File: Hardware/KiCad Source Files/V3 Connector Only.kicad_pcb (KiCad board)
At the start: 2 copper layers, 60 x 100 mm, 65 parts, among them J1 YK3210203000G, J2 USB4085-GF-A, J3 Conn_01x08, J4 YK3210203000G, J5 USB4085-GF-A, J6 USB1125-GF-B, Q1 IRLU024NPBF, Q2 IRLU024NPBF, Q3 Q_NMOS, U1 MC33063AP, U4 LM4040LP-2.0, U5 MCP4801, U6 MCP3202

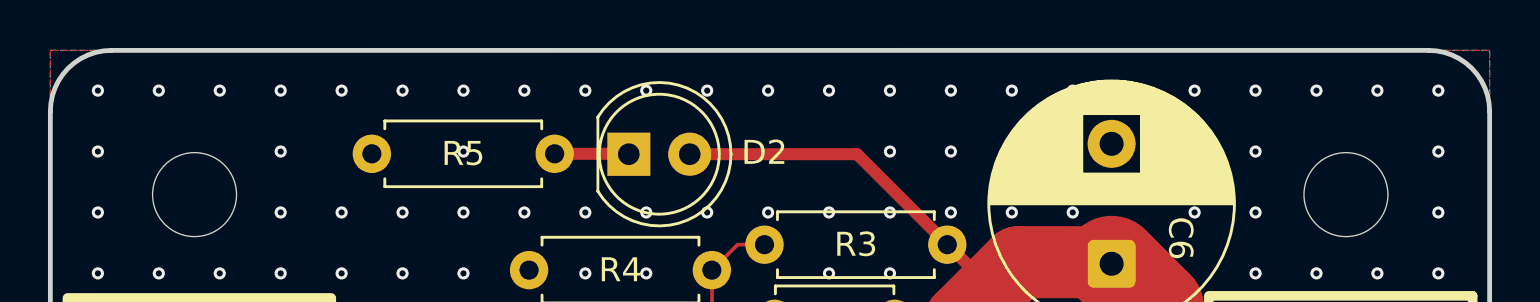
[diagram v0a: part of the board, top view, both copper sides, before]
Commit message: Remove R6 from BOM and Centroid files.
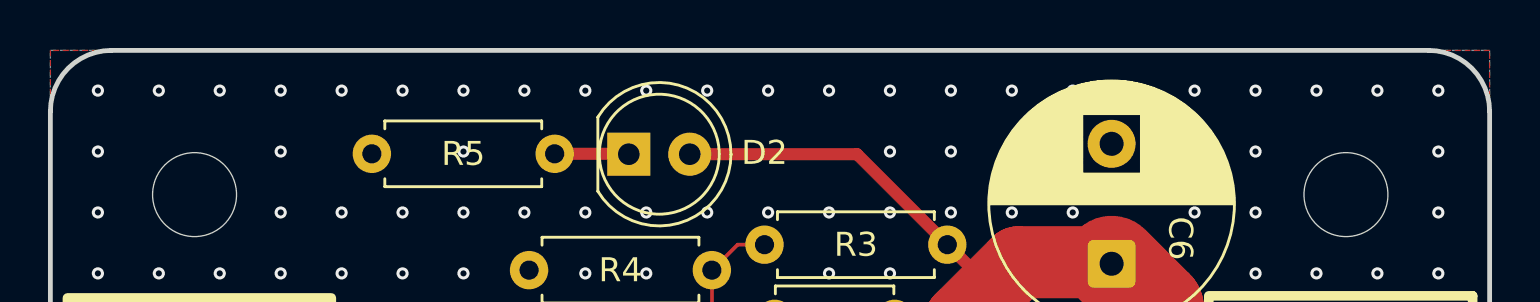
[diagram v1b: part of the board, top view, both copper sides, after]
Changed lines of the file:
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@@
 		(sheetname "/CC Sink/")
 		(sheetfile "Strobe Generation.kicad_sch")
-		(attr through_hole)
+		(attr through_hole dnp)
 		(fp_line
 			(start 7.08 -1.37)
@@
 		(layer "Edge.Cuts")
 	)
+	(gr_line
+		(start 62.737988 74.93)
+		(end 117.657928 74.93)
+		(stroke
+			(width 0.2)
+			(type solid)
+		)
+		(layer "Edge.Cuts")
+	)
 	(gr_arc
 		(start 60.198 77.47)
@@
 		)
 		(layer "Edge.Cuts")
-	)
-	(gr_line
-		(start 62.737988 74.93)
-		(end 117.665489 74.929065)
-		(stroke
-			(width 0.2)
-			(type solid)
-		)
-		(layer "Edge.Cuts")

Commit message: Finalized V3 Connector BOM based on testing on hardware.
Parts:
- R17: value 200R -> 1K
- R6: value 120R -> 1K
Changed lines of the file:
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@@
 			(drillshape 0)
 			(scaleselection 1)
-			(outputdirectory "V3 Connector Files/")
+			(outputdirectory "V3 Connector + IRLED Files/")
 		)
 	)
@@
 			)
 		)
-		(property "Value" "200R"
+		(property "Value" "1K"
 			(at 3.81 2.37 0)
 			(layer "F.Fab")
@@
 			)
 		)
-		(property "Part Number" "MFR-25FRF52-200R"
+		(property "Part Number" "MFR-25FRF52-1K"
 			(at 0 0 0)
 			(unlocked yes)
@@
 			)
 		)
-		(property "Value" "120R"
+		(property "Value" "1K"
 			(at 3.81 2.37 90)
 			(layer "F.Fab")
@@
 			)
 		)
-		(property "Part Number" "MFR-25FTE52-120R"
+		(property "Part Number" "MFR-25FRF52-1K"
 			(at 0 0 90)
 			(unlocked yes)
@@
 		(sheetname "/CC Sink/")
 		(sheetfile "Strobe Generation.kicad_sch")
-		(attr through_hole dnp)
+		(attr through_hole)
 		(fp_line
 			(start 7.08 -1.37)
@@
 		(sheetname "/CC Sink/")
 		(sheetfile "Strobe Generation.kicad_sch")
-		(attr through_hole)
+		(attr through_hole dnp)
 		(fp_line
 			(start 7.08 1.37)
@@
 		(sheetname "/CC Sink/")
 		(sheetfile "Strobe Generation.kicad_sch")
-		(attr through_hole)
+		(attr through_hole dnp)
 		(fp_line
 			(start 6.580001 0)
@@
 	)
 	(gr_line
-		(start 62.737988 74.93)
+		(start 62.738 74.929998)
 		(end 117.657928 74.93)
 		(stroke
@@
 		(stroke
 			(width 0.2)
-			(type default)
+			(type solid)
 		)
 		(layer "Edge.Cuts")
